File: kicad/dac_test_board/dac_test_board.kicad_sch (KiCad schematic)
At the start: 42 parts, among them J1 Power, J2 Vcca_select, J3 In_Hi, J4 In_Lo, J5 Out_Hi, J6 Out_Lo, J7 Vccb_select, J9 Signals, U1 MCP4725A2T-E/CH, U2 SN74LVC8T245

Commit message: pcb initial layout
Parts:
- added C4: 1u, Capacitor_SMD:C_0603_1608Metric_Pad1.08x0.95mm_HandSolder, symbol Device:C_Small
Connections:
- net +3V3: no longer C3.1
- net GND: now also C4.2
- net Vcca: now also C4.1
- net Vccb: now also C3.1
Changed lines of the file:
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@@
 	)
 	(symbol
+		(lib_id "power:GND")
+		(at 127 59.69 0)
+		(mirror y)
+		(unit 1)
+		(exclude_from_sim no)
+		(in_bom yes)
+		(on_board yes)
+		(dnp no)
+		(fields_autoplaced yes)
+		(property "Reference" "#PWR028"
+			(at 127 66.04 0)
+			(effects
+				(font
+					(size 1.27 1.27)
+				)
+				(hide yes)
+			)
+		)
+		(property "Value" "GND"
+			(at 127 64.77 0)
+			(effects
+				(font
+					(size 1.27 1.27)
+				)
+			)
+		)
+		(property "Footprint" ""
+			(at 127 59.69 0)
+			(effects
+				(font
+					(size 1.27 1.27)
+				)
+				(hide yes)
+			)
+		)
+		(property "Datasheet" ""
+			(at 127 59.69 0)
+			(effects
+				(font
+					(size 1.27 1.27)
+				)
+				(hide yes)
+			)
+		)
+		(property "Description" "Power symbol creates a global label with name \"GND\" , ground"
+			(at 127 59.69 0)
+			(effects
+				(font
+					(size 1.27 1.27)
+				)
+				(hide yes)
+			)
+		)
+		(pin "1"
+		)
+		(instances
+			(project "dac_test_board"
+				(path "/ff2d333f-f930-4a4f-b319-0ac06bf28c7c"
+					(reference "#PWR028")
+					(unit 1)
+				)
+			)
+		)
+	)
+	(symbol
 		(lib_id "power:+3V3")
 		(at 151.13 71.12 0)
@@
 	)
 	(symbol
+		(lib_id "power:+3V3")
+		(at 127 54.61 0)
+		(mirror y)
+		(unit 1)
+		(exclude_from_sim no)
+		(in_bom yes)
+		(on_board yes)
+		(dnp no)
+		(fields_autoplaced yes)
+		(property "Reference" "#PWR027"
+			(at 127 58.42 0)
+			(effects
+				(font
+					(size 1.27 1.27)
+				)
+				(hide yes)
+			)
+		)
+		(property "Value" "Vcca"
+			(at 127 49.53 0)
+			(effects
+				(font
+					(size 1.27 1.27)
+				)
+			)
+		)
+		(property "Footprint" ""
+			(at 127 54.61 0)
+			(effects
+				(font
+					(size 1.27 1.27)
+				)
+				(hide yes)
+			)
+		)
+		(property "Datasheet" ""
+			(at 127 54.61 0)
+			(effects
+				(font
+					(size 1.27 1.27)
+				)
+				(hide yes)
+			)
+		)
+		(property "Description" "Power symbol creates a global label with name \"+3V3\""
+			(at 127 54.61 0)
+			(effects
+				(font
+					(size 1.27 1.27)
+				)
+				(hide yes)
+			)
+		)
+		(pin "1"
+		)
+		(instances
+			(project "dac_test_board"
+				(path "/ff2d333f-f930-4a4f-b319-0ac06bf28c7c"
+					(reference "#PWR027")
+					(unit 1)
+				)
+			)
+		)
+	)
+	(symbol
 		(lib_id "power:GND")
 		(at 157.48 176.53 0)
@@
 	)
 	(symbol
+		(lib_id "Device:C_Small")
+		(at 127 57.15 0)
+		(mirror y)
+		(unit 1)
+		(exclude_from_sim no)
+		(in_bom yes)
+		(on_board yes)
+		(dnp no)
+		(fields_autoplaced yes)
+		(property "Reference" "C4"
+			(at 124.46 55.8863 0)
+			(effects
+				(font
+					(size 1.27 1.27)
+				)
+				(justify left)
+			)
+		)
+		(property "Value" "1u"
+			(at 124.46 58.4263 0)
+			(effects
+				(font
+					(size 1.27 1.27)
+				)
+				(justify left)
+			)
+		)
+		(property "Footprint" "Capacitor_SMD:C_0603_1608Metric_Pad1.08x0.95mm_HandSolder"
+			(at 127 57.15 0)
+			(effects
+				(font
+					(size 1.27 1.27)
+				)
+				(hide yes)
+			)
+		)
+		(property "Datasheet" "~"
+			(at 127 57.15 0)
+			(effects
+				(font
+					(size 1.27 1.27)
+				)
+				(hide yes)
+			)
+		)
+		(property "Description" ""
+			(at 127 57.15 0)
+			(effects
+				(font
+					(size 1.27 1.27)
+				)
+				(hide yes)
+			)
+		)
+		(pin "1"
+		)
+		(pin "2"
+		)
+		(instances
+			(project "dac_test_board"
+				(path "/ff2d333f-f930-4a4f-b319-0ac06bf28c7c"
+					(reference "C4")
+					(unit 1)
+				)
+			)
+		)
+	)
+	(symbol
 		(lib_id "Device:R_Small")
 		(at 158.75 76.2 180)
@@
 	(symbol
 		(lib_id "power:+3V3")
+		(at 58.42 54.61 0)
+		(unit 1)
+		(exclude_from_sim no)
+		(in_bom yes)
+		(on_board yes)
+		(dnp no)
+		(fields_autoplaced yes)
+		(property "Reference" "#PWR014"
+			(at 58.42 58.42 0)
+			(effects
+				(font
+					(size 1.27 1.27)
+				)
+				(hide yes)
+			)
+		)
+		(property "Value" "Vccb"
+			(at 58.42 49.53 0)
+			(effects
+				(font
+					(size 1.27 1.27)
+				)
+			)
+		)
+		(property "Footprint" ""
+			(at 58.42 54.61 0)
+			(effects
+				(font
+					(size 1.27 1.27)
+				)
+				(hide yes)
+			)
+		)
+		(property "Datasheet" ""
+			(at 58.42 54.61 0)
+			(effects
+				(font
+					(size 1.27 1.27)
+				)
+				(hide yes)
+			)
+		)
+		(property "Description" "Power symbol creates a global label with name \"+3V3\""
+			(at 58.42 54.61 0)
+			(effects
+				(font
+					(size 1.27 1.27)
+				)
+				(hide yes)
+			)
+		)
+		(pin "1"
+		)
+		(instances
+			(project "dac_test_board"
+				(path "/ff2d333f-f930-4a4f-b319-0ac06bf28c7c"
+					(reference "#PWR014")
+					(unit 1)
+				)
+			)
+		)
+	)
+	(symbol
+		(lib_id "power:+3V3")
 		(at 111.76 54.61 0)
 		(mirror y)
@@
 					(unit 1)
 				)
-			)
-		)
-	)
-	(symbol
-		(lib_id "power:+3V3")
-		(at 58.42 54.61 0)
-		(mirror y)
-		(unit 1)
-		(exclude_from_sim no)
-		(in_bom yes)
-		(on_board yes)
-		(dnp no)
-		(fields_autoplaced yes)
-		(property "Reference" "#PWR014"
-			(at 58.42 58.42 0)
-			(effects
-				(font
-					(size 1.27 1.27)
-				)
-				(hide yes)
-			)
-		)
-		(property "Value" "+3V3"
-			(at 58.42 49.53 0)
-			(effects
-				(font
-					(size 1.27 1.27)
-				)
-			)
-		)
-		(property "Footprint" ""
-			(at 58.42 54.61 0)
-			(effects
-				(font
-					(size 1.27 1.27)
-				)
-				(hide yes)
-			)
-		)
-		(property "Datasheet" ""
-			(at 58.42 54.61 0)
-			(effects
-				(font
-					(size 1.27 1.27)
-				)
-				(hide yes)
-			)
-		)
-		(property "Description" "Power symbol creates a global label with name \"+3V3\""
-			(at 58.42 54.61 0)
-			(effects
-				(font
-					(size 1.27 1.27)
-				)
-				(hide yes)
-			)
-		)
-		(pin "1"
-		)
-		(instances
-			(project "dac_test_board"
-				(path "/ff2d333f-f930-4a4f-b319-0ac06bf28c7c"
-					(reference "#PWR014")
-					(unit 1)
-				)

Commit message: changed In pinout to put GND in middle and added stemma qt
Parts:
- added J8: JST_SH_BM04B-SRSS-TB, Connector_JST:JST_SH_BM04B-SRSS-TB_1x04-1MP_P1.00mm_Vertical, symbol Connector_Generic:Conn_01x04
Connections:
- net +3V3: now also J8.2 (Pin_2)
- net GND: now also J3.5 (Pin_5), J3.6 (Pin_6), J4.5 (Pin_5), J4.6 (Pin_6), J8.1 (Pin_1); no longer J3.1 (Pin_1), J3.2 (Pin_2), J4.1 (Pin_1), J4.2 (Pin_2)
- net I2C1_SCL: now also J8.4 (Pin_4)
- net I2C1_SDA: now also J8.3 (Pin_3)
- net IN00: now also J4.1 (Pin_1), J4.2 (Pin_2); no longer J4.3 (Pin_3), J4.4 (Pin_4)
- net IN01: now also J4.3 (Pin_3), J4.4 (Pin_4); no longer J4.5 (Pin_5), J4.6 (Pin_6)
- net IN04: now also J3.1 (Pin_1), J3.2 (Pin_2); no longer J3.3 (Pin_3), J3.4 (Pin_4)
- net IN05: now also J3.3 (Pin_3), J3.4 (Pin_4); no longer J3.5 (Pin_5), J3.6 (Pin_6)
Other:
- note added: "Stemma QT"

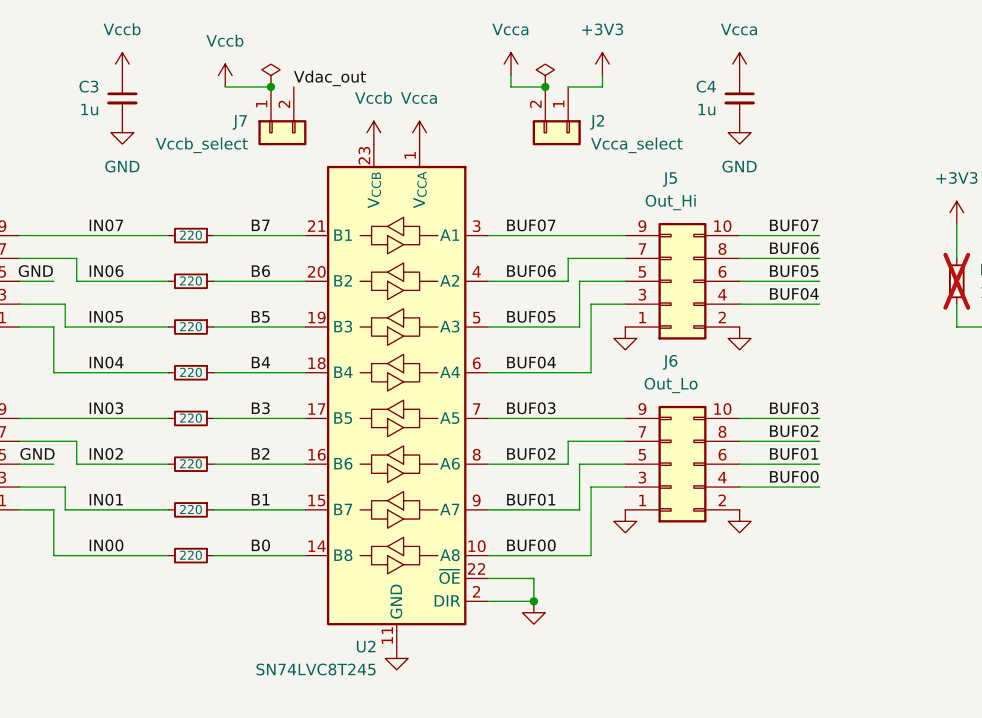
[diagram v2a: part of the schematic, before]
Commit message: forgot the ldo... :(
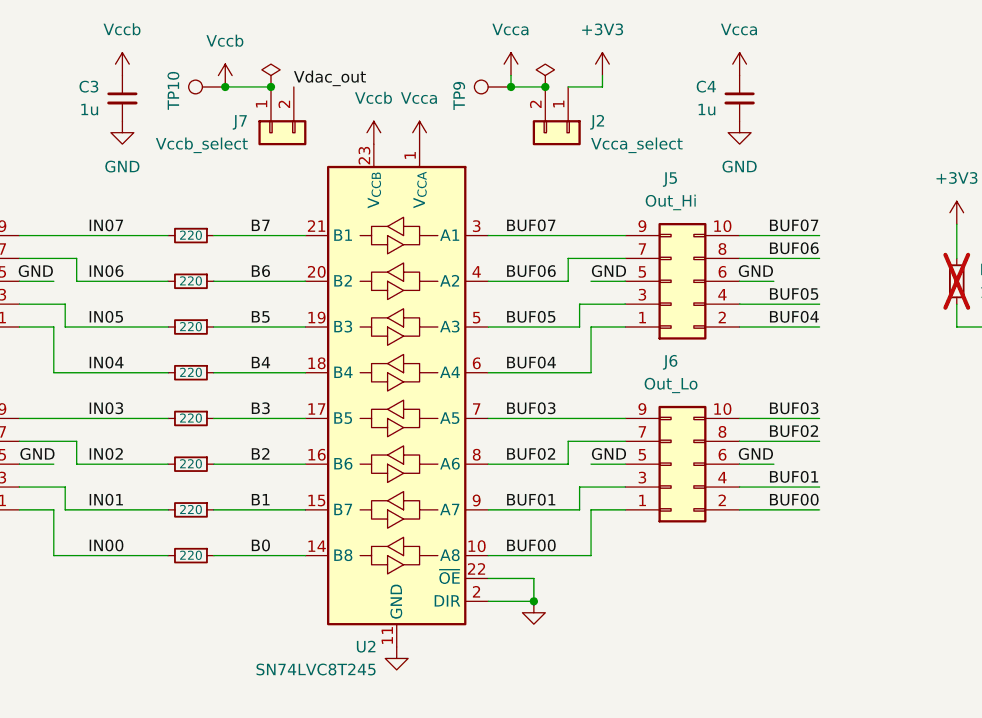
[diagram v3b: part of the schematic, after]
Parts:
- added TP10, TP9: TestPoint_Harwin, My Libraries:Harwin-S1751-46-Test-Point, symbol My Library:TestPoint_Harwin
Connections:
- net BUF00: now also J6.1 (Pin_1), J6.2 (Pin_2); no longer J6.3 (Pin_3), J6.4 (Pin_4)
- net BUF01: now also J6.3 (Pin_3), J6.4 (Pin_4); no longer J6.5 (Pin_5), J6.6 (Pin_6)
- net BUF04: now also J5.1 (Pin_1), J5.2 (Pin_2); no longer J5.3 (Pin_3), J5.4 (Pin_4)
- net BUF05: now also J5.3 (Pin_3), J5.4 (Pin_4); no longer J5.5 (Pin_5), J5.6 (Pin_6)
- net GND: now also J5.5 (Pin_5), J5.6 (Pin_6), J6.5 (Pin_5), J6.6 (Pin_6); no longer J5.1 (Pin_1), J5.2 (Pin_2), J6.1 (Pin_1), J6.2 (Pin_2)
- net Vcca: now also TP9.1
- net Vccb: now also TP10.1

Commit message: splitting project
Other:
- note added: "Now.. I am thinking of the DigiPot and LDO on a single board. Then breakout for the buffer that connects to it."
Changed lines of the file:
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@@
+		)
+	)
+	(text "Now.. I am thinking of the DigiPot and LDO on a single board.\nThen breakout for the buffer that connects to it."
+		(exclude_from_sim no)
+		(at 218.44 137.16 0)
+		(effects
+			(font
+				(size 1.27 1.27)
+			)
 		)
 	)

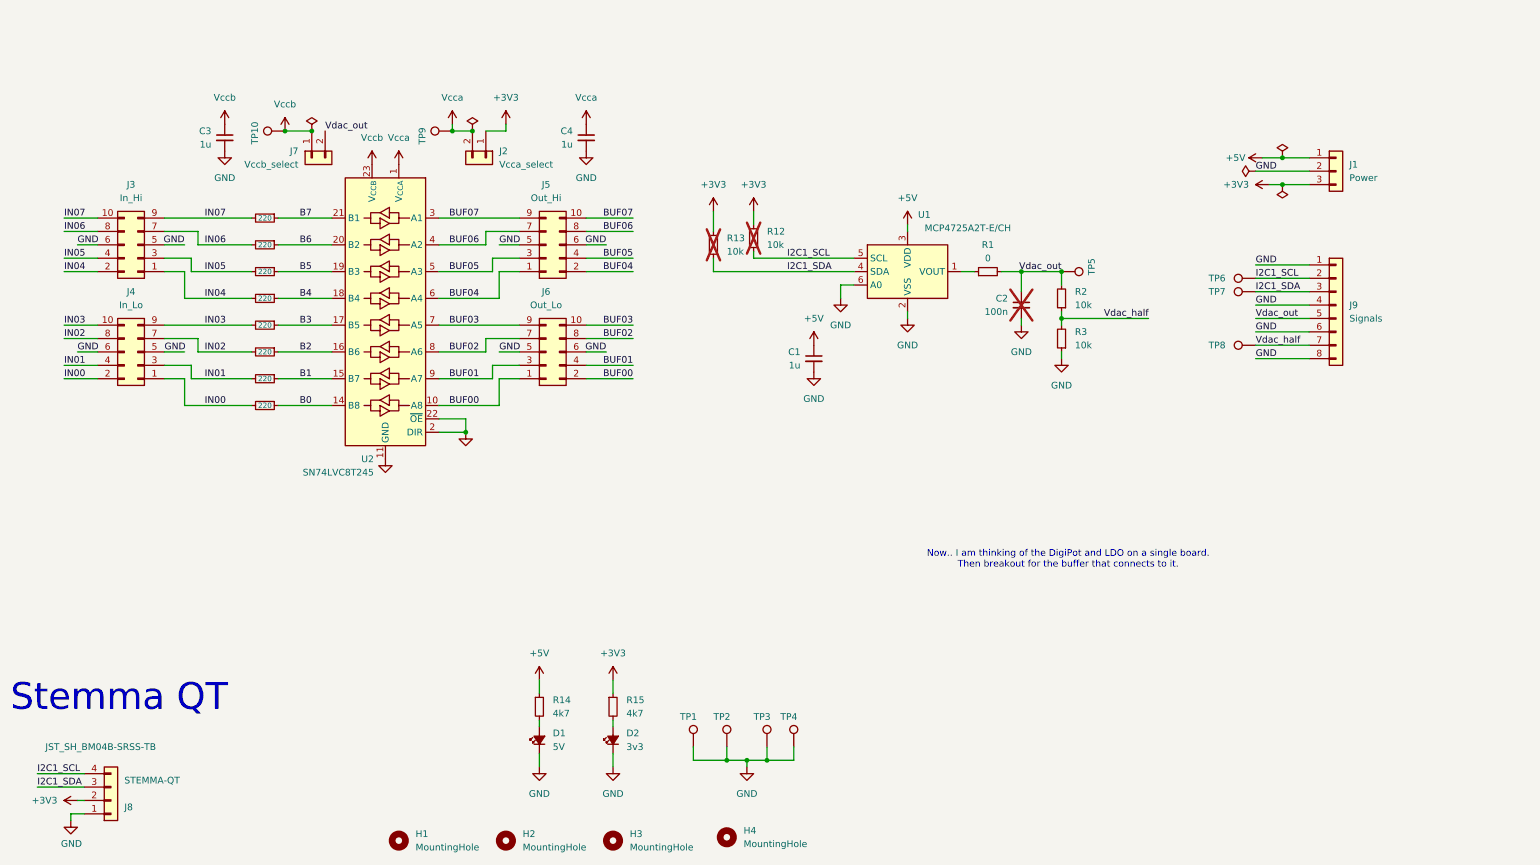
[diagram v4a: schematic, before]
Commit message: initial rip-up for dac only
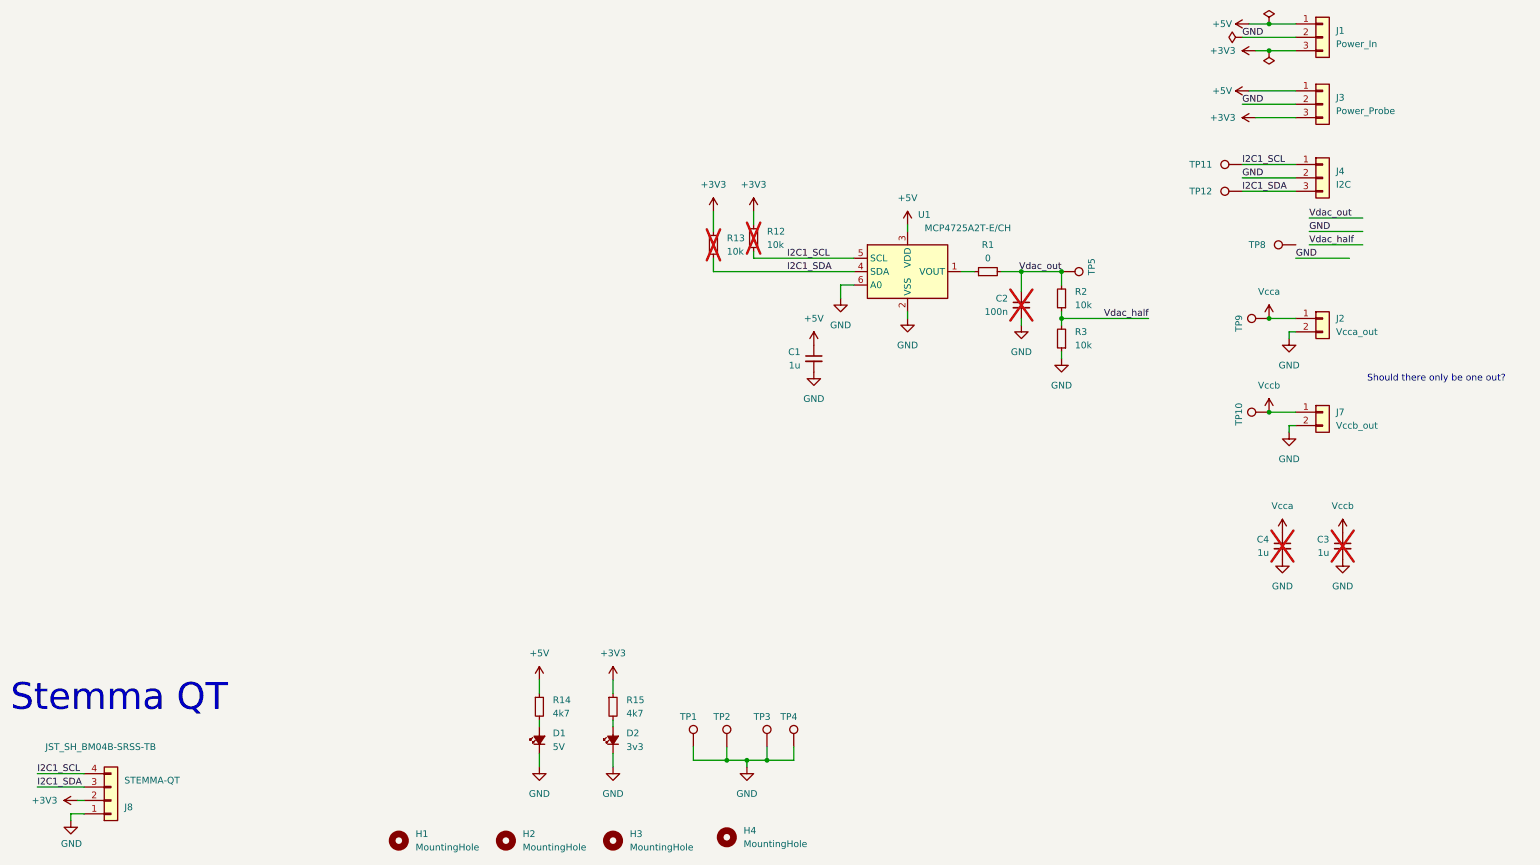
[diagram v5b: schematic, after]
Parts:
- removed J3: In_Hi, Connector_PinHeader_2.54mm:PinHeader_2x05_P2.54mm_Vertical, symbol Connector_Generic:Conn_02x05_Odd_Even
- removed J4: In_Lo, Connector_PinHeader_2.54mm:PinHeader_2x05_P2.54mm_Vertical, symbol Connector_Generic:Conn_02x05_Odd_Even
- removed J5: Out_Hi, Connector_PinHeader_2.54mm:PinHeader_2x05_P2.54mm_Vertical, symbol Connector_Generic:Conn_02x05_Odd_Even
- removed J6: Out_Lo, Connector_PinHeader_2.54mm:PinHeader_2x05_P2.54mm_Vertical, symbol Connector_Generic:Conn_02x05_Odd_Even
- removed J9: Signals, Connector_PinHeader_2.54mm:PinHeader_1x08_P2.54mm_Vertical, symbol Connector_Generic:Conn_01x08
- removed R10, R11, R4, R5, R6, R7, R8, R9: 220, Resistor_SMD:R_0603_1608Metric, symbol Device:R_Small
- removed TP6, TP7: TestPoint_Harwin, My Libraries:Harwin-S1751-46-Test-Point, symbol My Library:TestPoint_Harwin
- removed U2: SN74LVC8T245, Package_SO:SSOP-24_3.9x8.7mm_P0.635mm, symbol Logic_LevelTranslator:SN74LVC8T245
- added J3: Power_Probe, Connector_PinHeader_2.54mm:PinHeader_1x03_P2.54mm_Vertical, symbol Connector_Generic:Conn_01x03
- added J4: I2C, Connector_PinHeader_2.54mm:PinHeader_1x03_P2.54mm_Vertical, symbol Connector_Generic:Conn_01x03
- added TP11, TP12: TestPoint_Harwin, My Libraries:Harwin-S1751-46-Test-Point, symbol My Library:TestPoint_Harwin
- C3, C4: now not fitted
- J1: value Power -> Power_In
- J2: value Vcca_select -> Vcca_out
- J7: value Vccb_select -> Vccb_out
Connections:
- net +3V3: now also J3.3 (Pin_3); no longer J2.1 (Pin_1)
- net +5V: now also J3.1 (Pin_1)
- net GND: now also J2.2 (Pin_2), J7.2 (Pin_2), J3.2 (Pin_2), J4.2 (Pin_2)
- net I2C1_SCL: now also J4.1 (Pin_1), TP11.1
- net I2C1_SDA: now also J4.3 (Pin_3), TP12.1
- net Vcca: now also J2.1 (Pin_1); no longer J2.2 (Pin_2)
- net Vdac_half: no longer TP8.1
- net Vdac_out: no longer J7.2 (Pin_2)
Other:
- note added: "Should there only be one out?"
- note removed: "Now.. I am thinking of the DigiPot and LDO on a single board. Then breakout for the buffer that connects to it."
- moved on the sheet: J1, J2, J7, TP10, TP8, TP9

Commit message: pcb passes drc
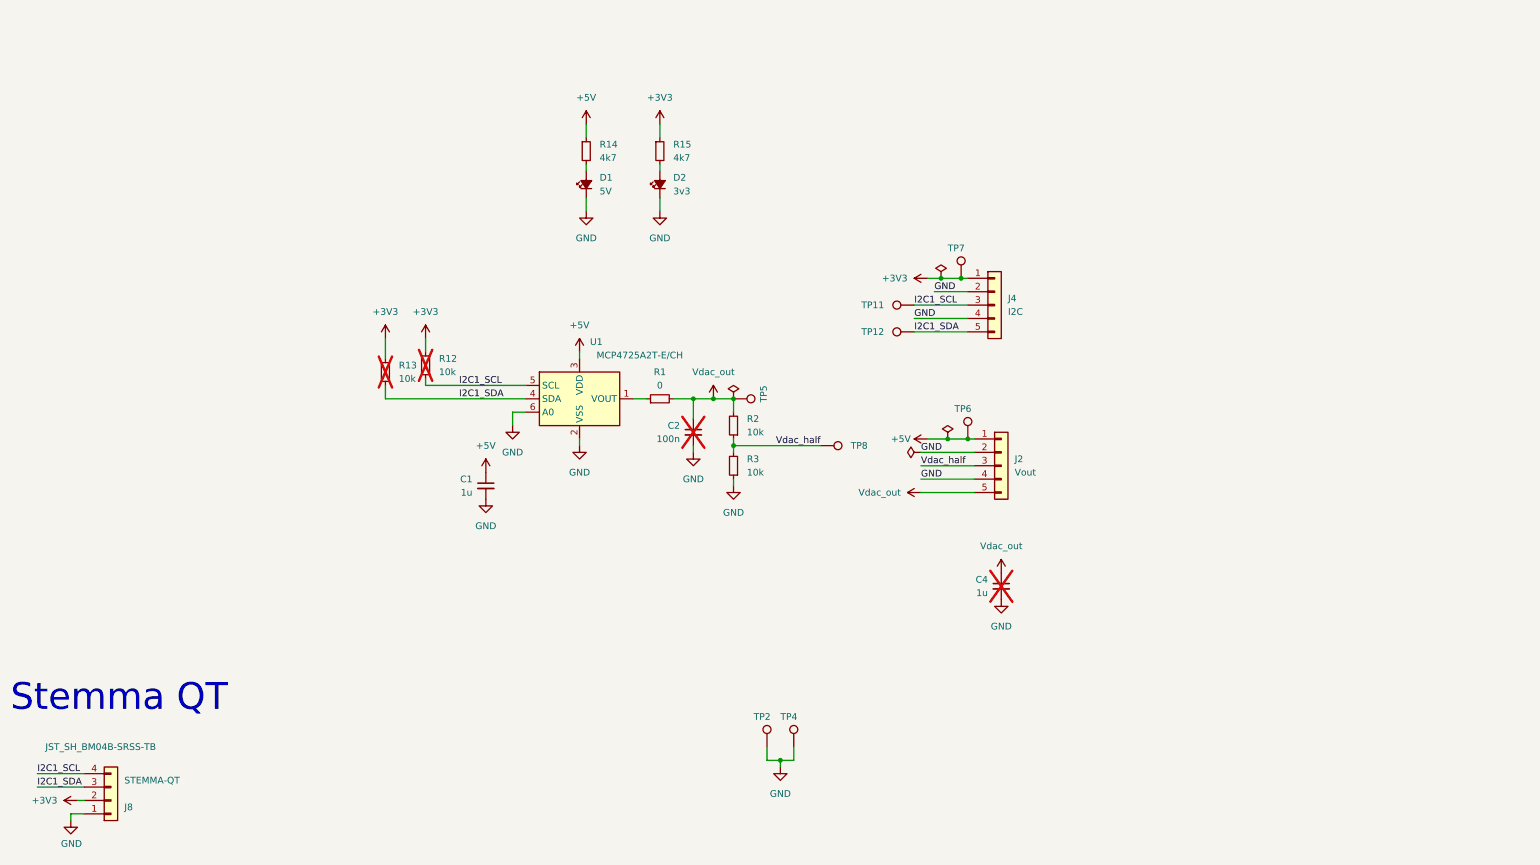
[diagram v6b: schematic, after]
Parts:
- removed C3: 1u, Capacitor_SMD:C_0603_1608Metric_Pad1.08x0.95mm_HandSolder, symbol Device:C_Small
- removed H1, H2, H3, H4: MountingHole, MountingHole:MountingHole_2.7mm, symbol Mechanical:MountingHole
- removed J1: Power_In, Connector_PinHeader_2.54mm:PinHeader_1x03_P2.54mm_Vertical, symbol Connector_Generic:Conn_01x03
- removed J2: Vcca_out, Connector_PinHeader_2.54mm:PinHeader_2x01_P2.54mm_Vertical, symbol Connector_Generic:Conn_01x02
- removed J3: Power_Probe, Connector_PinHeader_2.54mm:PinHeader_1x03_P2.54mm_Vertical, symbol Connector_Generic:Conn_01x03
- removed J7: Vccb_out, Connector_PinHeader_2.54mm:PinHeader_2x01_P2.54mm_Vertical, symbol Connector_Generic:Conn_01x02
- removed TP1, TP10, TP3, TP9: TestPoint_Harwin, My Libraries:Harwin-S1751-46-Test-Point, symbol My Library:TestPoint_Harwin
- added J2: Vout, Connector_PinHeader_2.54mm:PinHeader_1x05_P2.54mm_Vertical, symbol Connector_Generic:Conn_01x05
- added TP6, TP7: TestPoint_Harwin, My Libraries:Harwin-S1751-46-Test-Point, symbol My Library:TestPoint_Harwin
- J4: footprint Connector_PinHeader_2.54mm:PinHeader_1x03_P2.54mm_Vertical -> Connector_PinHeader_2.54mm:PinHeader_1x05_P2.54mm_Vertical; symbol Connector_Generic:Conn_01x03 -> Connector_Generic:Conn_01x05
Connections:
- net Vcca is gone; now on net Vdac_out: C4.1
- net +3V3: now also J4.1 (Pin_1), TP7.1
- net +5V: now also J2.1 (Pin_1), TP6.1
- net GND: now also J4.4 (Pin_4), J2.2 (Pin_2), J2.4 (Pin_4)
- net I2C1_SCL: now also J4.3 (Pin_3); no longer J4.1 (Pin_1)
- net I2C1_SDA: now also J4.5 (Pin_5); no longer J4.3 (Pin_3)
- net Vdac_half: now also TP8.1, J2.3 (Pin_3)
- net Vdac_out: now also J2.5 (Pin_5)
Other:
- note removed: "Should there only be one out?"
- moved on the sheet: C1, C2, C4, D1, D2, R1, R12, R13, R14, R15, R2, R3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
